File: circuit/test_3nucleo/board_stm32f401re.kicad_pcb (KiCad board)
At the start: 2 copper layers, 76.1 x 78.2 mm, 29 parts, among them SW1 SW_Push, SW2 SW_Push, SW3 SW_Push, U1 NUCLEO-64, U2 MAX98357_DAC

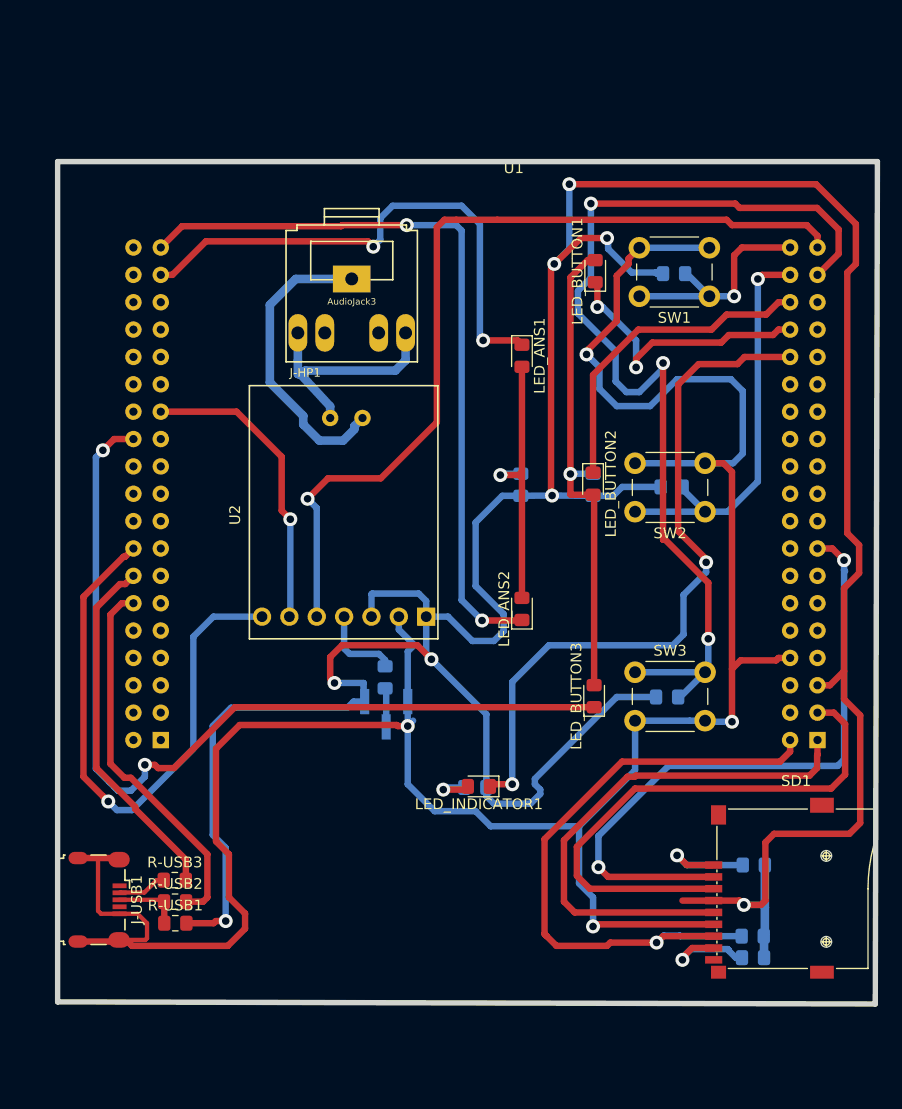
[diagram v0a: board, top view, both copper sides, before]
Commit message: add ESP on board module
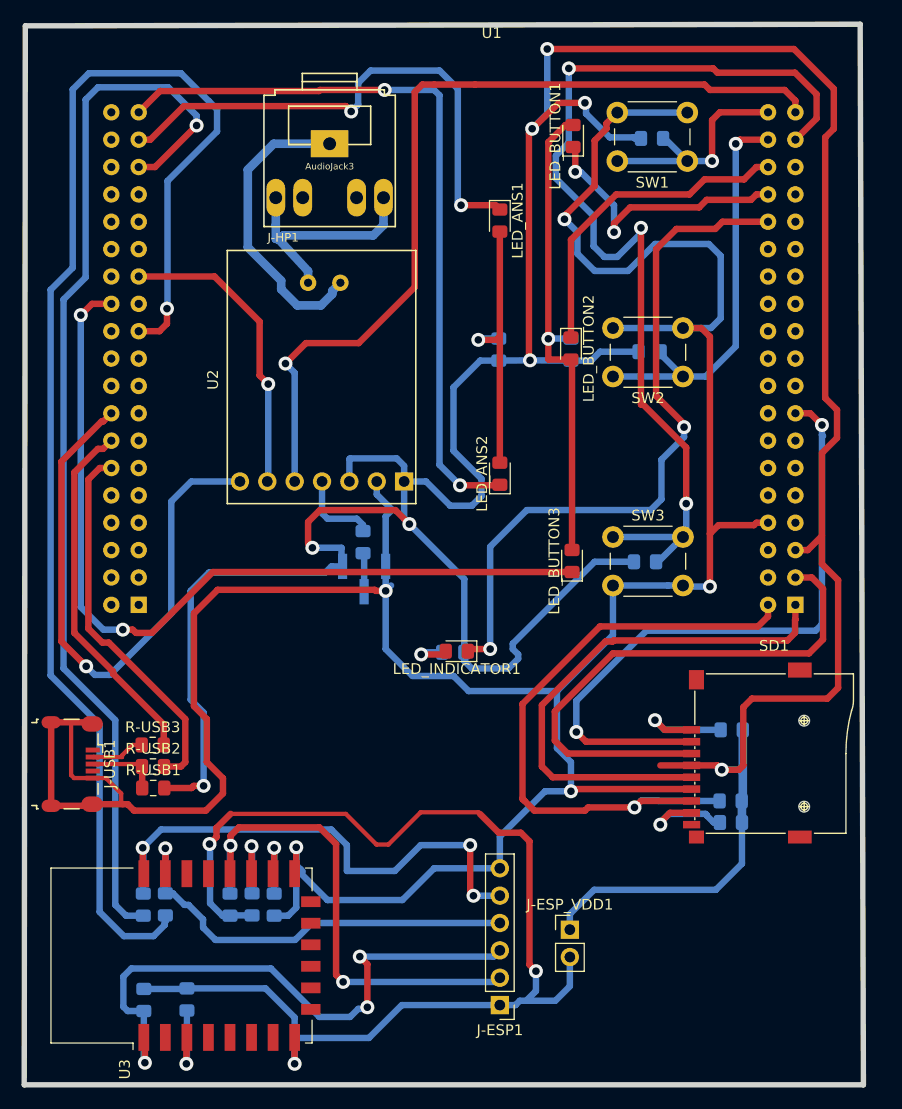
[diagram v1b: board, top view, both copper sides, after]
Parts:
- added J-ESP1: Conn_01x06_Male, Connector_PinHeader_2.54mm:PinHeader_1x06_P2.54mm_Vertical, F.Cu at (142.8, 128.9)
- added J-ESP_VDD1: Conn_01x02_Male, Connector_PinHeader_2.54mm:PinHeader_1x02_P2.54mm_Vertical, F.Cu at (149.2, 121.9)
- added R-ESP1: 4K7, Resistor_SMD:R_0805_2012Metric_Pad1.15x1.40mm_HandSolder, B.Cu at (117.7, 119.6)
- added R-ESP2: 4K7, Resistor_SMD:R_0805_2012Metric_Pad1.15x1.40mm_HandSolder, B.Cu at (119.8, 119.5)
- added R-ESP3: 4K7, Resistor_SMD:R_0805_2012Metric_Pad1.15x1.40mm_HandSolder, B.Cu at (113.7, 128.4)
- added R-ESP4: 4K7, Resistor_SMD:R_0805_2012Metric_Pad1.15x1.40mm_HandSolder, B.Cu at (109.7, 128.4)
- added R-ESP5: 4K7, Resistor_SMD:R_0805_2012Metric_Pad1.15x1.40mm_HandSolder, B.Cu at (121.8, 119.6)
- added R-IOT1: 0, Resistor_SMD:R_0805_2012Metric_Pad1.15x1.40mm_HandSolder, B.Cu at (109.7, 119.6)
- added R-IOT2: 0, Resistor_SMD:R_0805_2012Metric_Pad1.15x1.40mm_HandSolder, B.Cu at (111.7, 119.5)
- added U3: ESP-12E, RF_Module:ESP-12E, F.Cu at (113.2, 124.3)
- moved G*** 16.1 mm to (129.4, 101.5)
- moved J-USB1 12.8 mm to (103.0, 106.5)
- moved U2 12.7 mm to (126.5, 70.8)
- moved J-GAIN1 12.7 mm to (130.2, 89.3)
- moved R-SD1 12.7 mm to (164.3, 103.3)
- moved J-HP1 12.7 mm to (127.0, 50.5)
- moved SW1 12.7 mm to (160.2, 50.5)
- moved LED_ANS1 12.7 mm to (142.8, 56.1)
- moved LED_ANS2 12.7 mm to (142.8, 79.6)
- moved LED_BUTTON2 12.7 mm to (149.3, 68.0)
- moved LED_BUTTON3 12.7 mm to (149.4, 87.7)
- moved LED_INDICATOR1 12.7 mm to (138.8, 96.0)
- moved R-BTN1 12.7 mm to (156.9, 48.5)
- moved R-BTN3 12.7 mm to (156.2, 87.8)
- moved R-LED2 12.7 mm to (149.3, 68.0)
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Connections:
- U1 pad 59: Net-(U1-Pad59) -> /TXD
- U1 pad 71: Net-(U1-Pad71) -> /RXD
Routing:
- net /TXD: track 0.00 -> 127.5 mm, vias 0 -> 1
- net /ESP_VDD: track 0.00 -> 112.4 mm, vias 0 -> 3
- net /RXD: track 0.00 -> 100.4 mm, vias 0 -> 1
- net /ESP_RST: track 0.00 -> 56.2 mm, vias 0 -> 3
- net GND: track 233.2 -> 284.8 mm, vias 4 -> 5
- net /ESP_TXD: track 0.00 -> 49.1 mm, vias 0 -> 3
- net /ESP_P0: track 0.00 -> 46.7 mm, vias 0 -> 2
- net /ESP_RXD: track 0.00 -> 40.5 mm, vias 0 -> 1
- net VDD: track 308.3 -> 331.5 mm
- net /ESP_EN: track 0.00 -> 7.44 mm, vias 0 -> 1
- net /ESP_P2: track 0.00 -> 6.95 mm, vias 0 -> 1
- net /ESP_P15: track 0.00 -> 6.69 mm, vias 0 -> 1
- net /LED_C: track 84.3 -> 79.3 mm
- net Net-(J-USB1-Pad3): track 6.21 -> 6.93 mm
- net Net-(J-USB1-Pad2): track 4.59 -> 5.21 mm
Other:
- board size 76.1 x 78.2 mm -> 77.9 x 98.5 mm

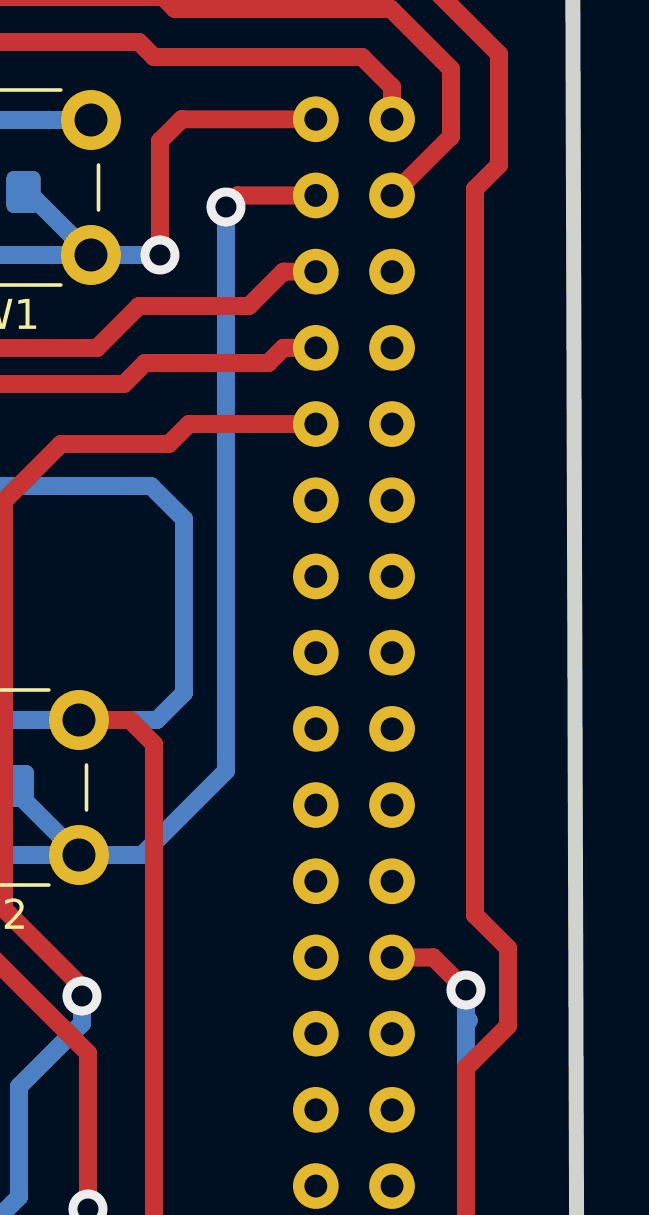
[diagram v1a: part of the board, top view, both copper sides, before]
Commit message: MMC_NSS on PA.15 not PA.14 you IDIOT!!!
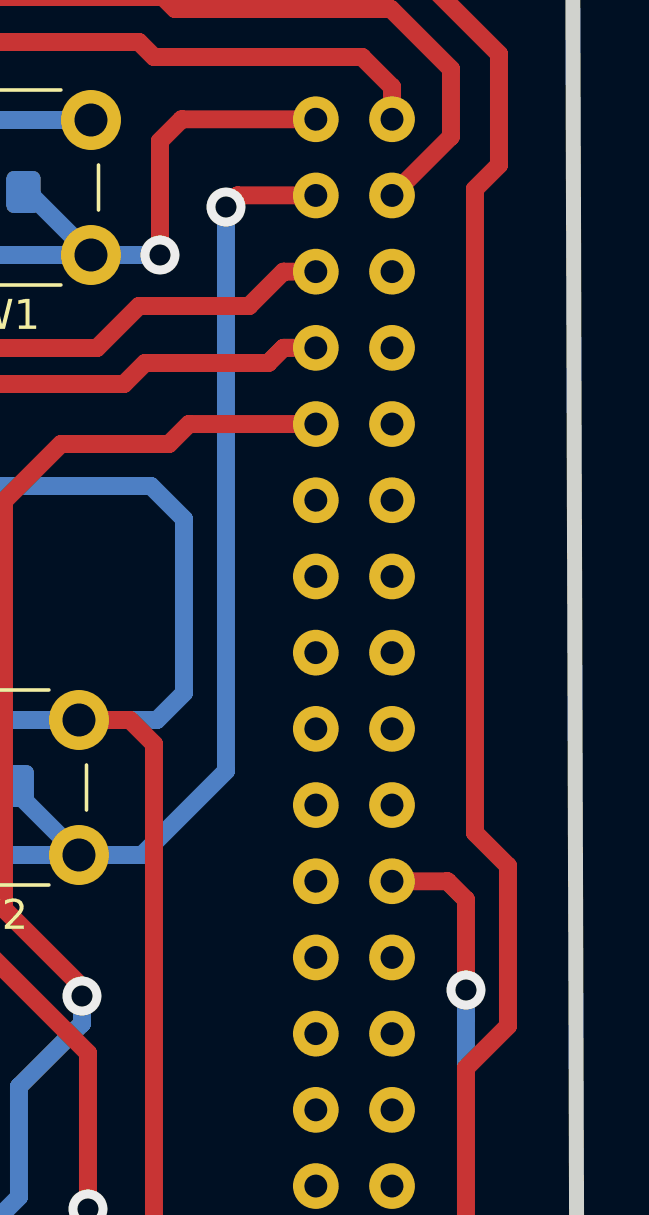
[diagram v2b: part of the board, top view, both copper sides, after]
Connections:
- U1 pad 15: /MMC_NSS -> Net-(U1-Pad15)
- U1 pad 17: Net-(U1-Pad17) -> /MMC_NSS
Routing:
- net /MMC_NSS: track 61.3 -> 63.9 mm
